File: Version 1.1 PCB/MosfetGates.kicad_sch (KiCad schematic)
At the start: 27 parts, among them Q1 N_FET_ISC0602NLS, Q2 N_FET_ISC0602NLS

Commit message: Added ESD protection and test pins
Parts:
- TP19, TP22, TP25, TP? (x6): footprint FootPrint_ESC:PAD_TP -> easyeda2kicad:SMD_RH-5015

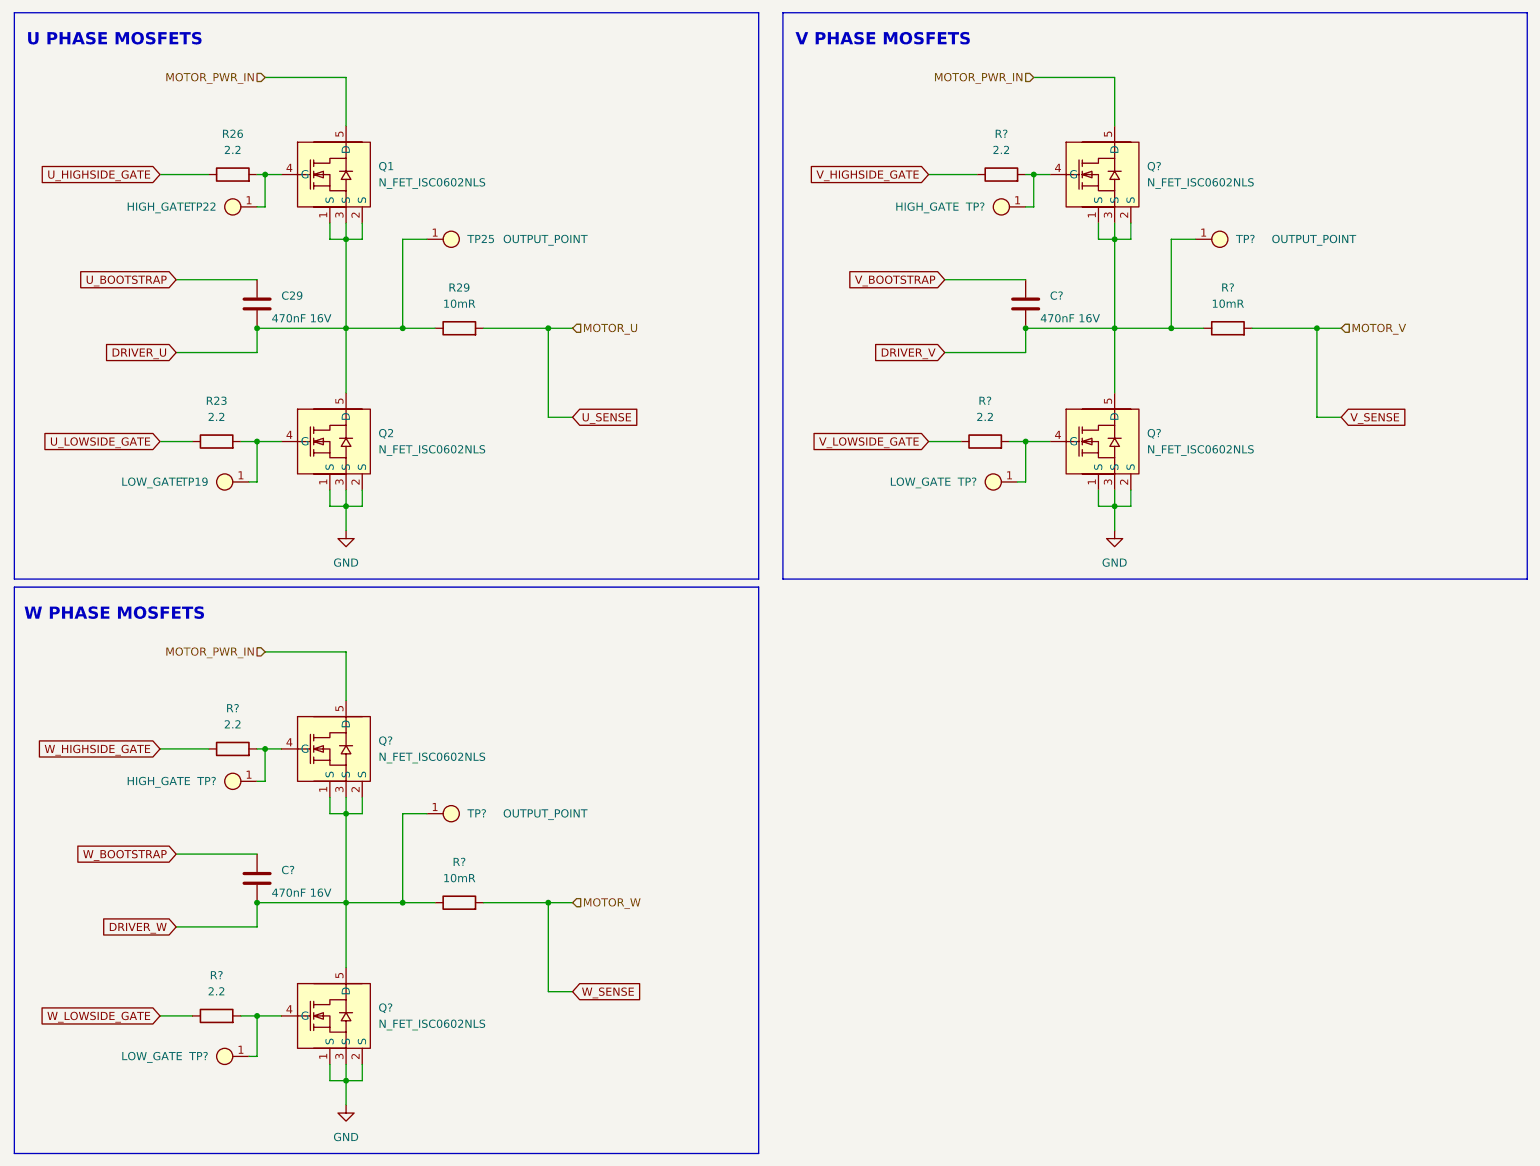
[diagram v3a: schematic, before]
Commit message: began part placement
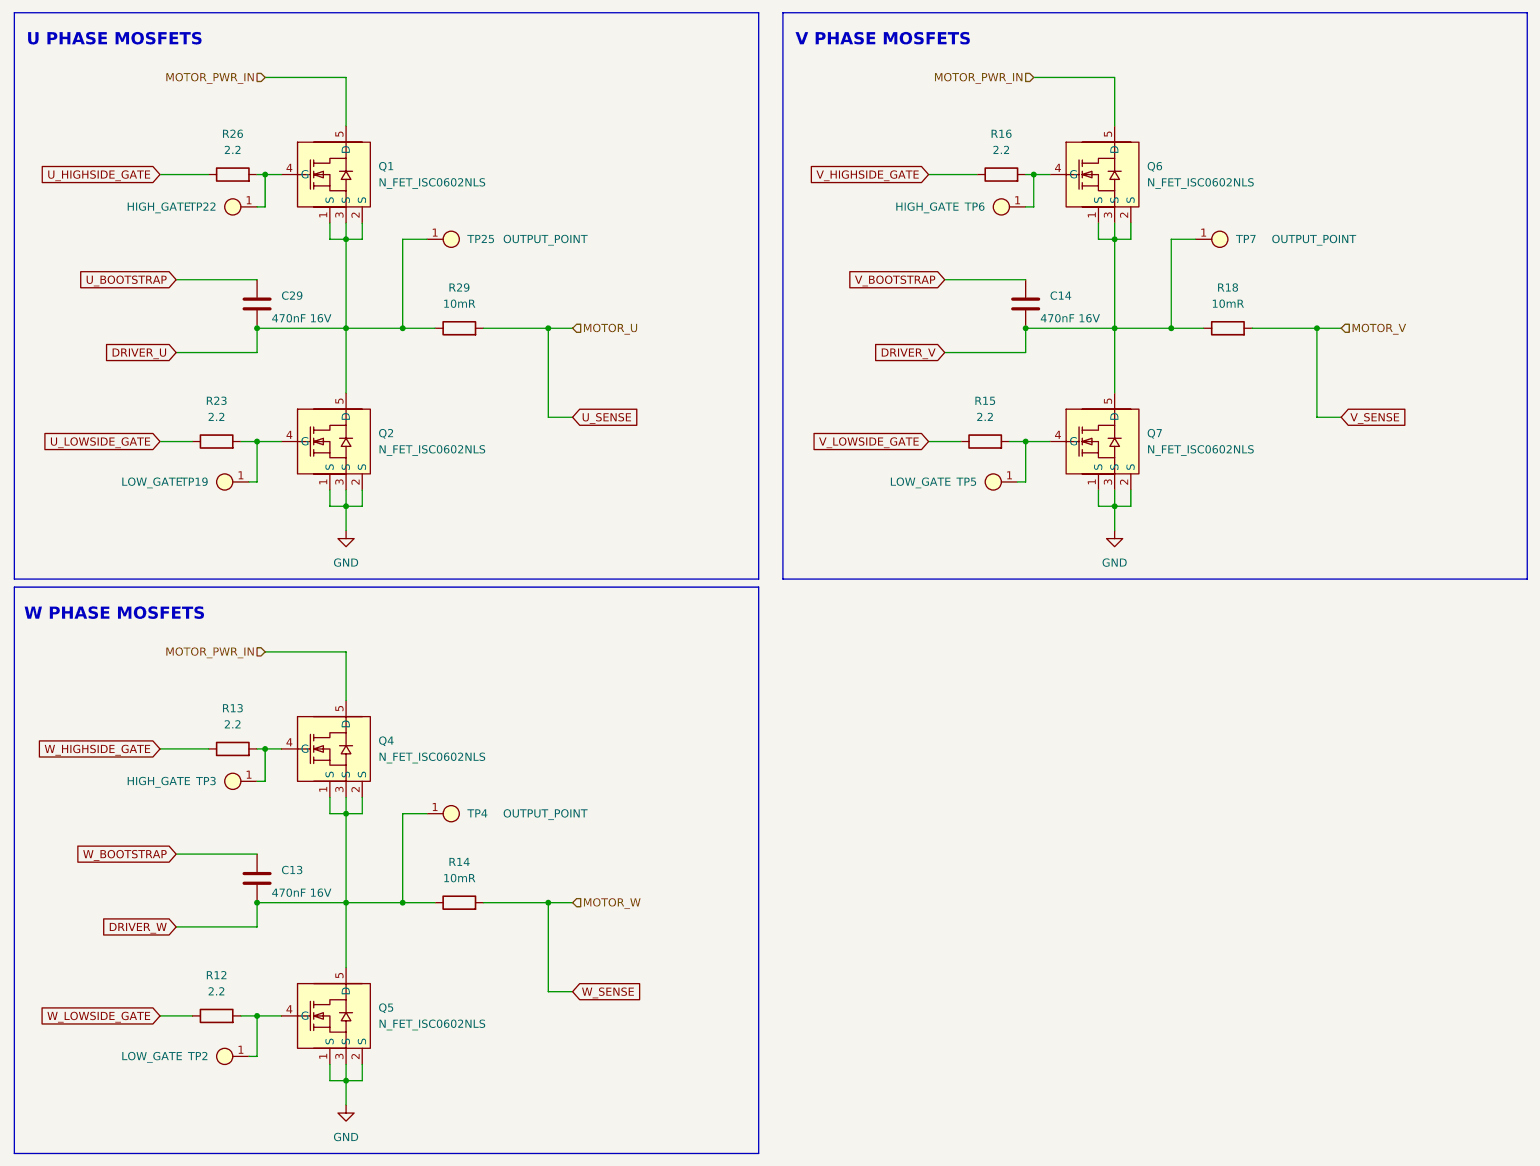
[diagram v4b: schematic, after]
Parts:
- gave numbers to parts that had none: 18
